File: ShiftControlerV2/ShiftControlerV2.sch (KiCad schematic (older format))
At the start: 24 parts, among them J1 Conn_02x06_Counter_Clockwise, J2 Conn_02x06_Counter_Clockwise, Q1 BTN8982TA, Q2 BTN8982TA, U1 ControllerBoardV2

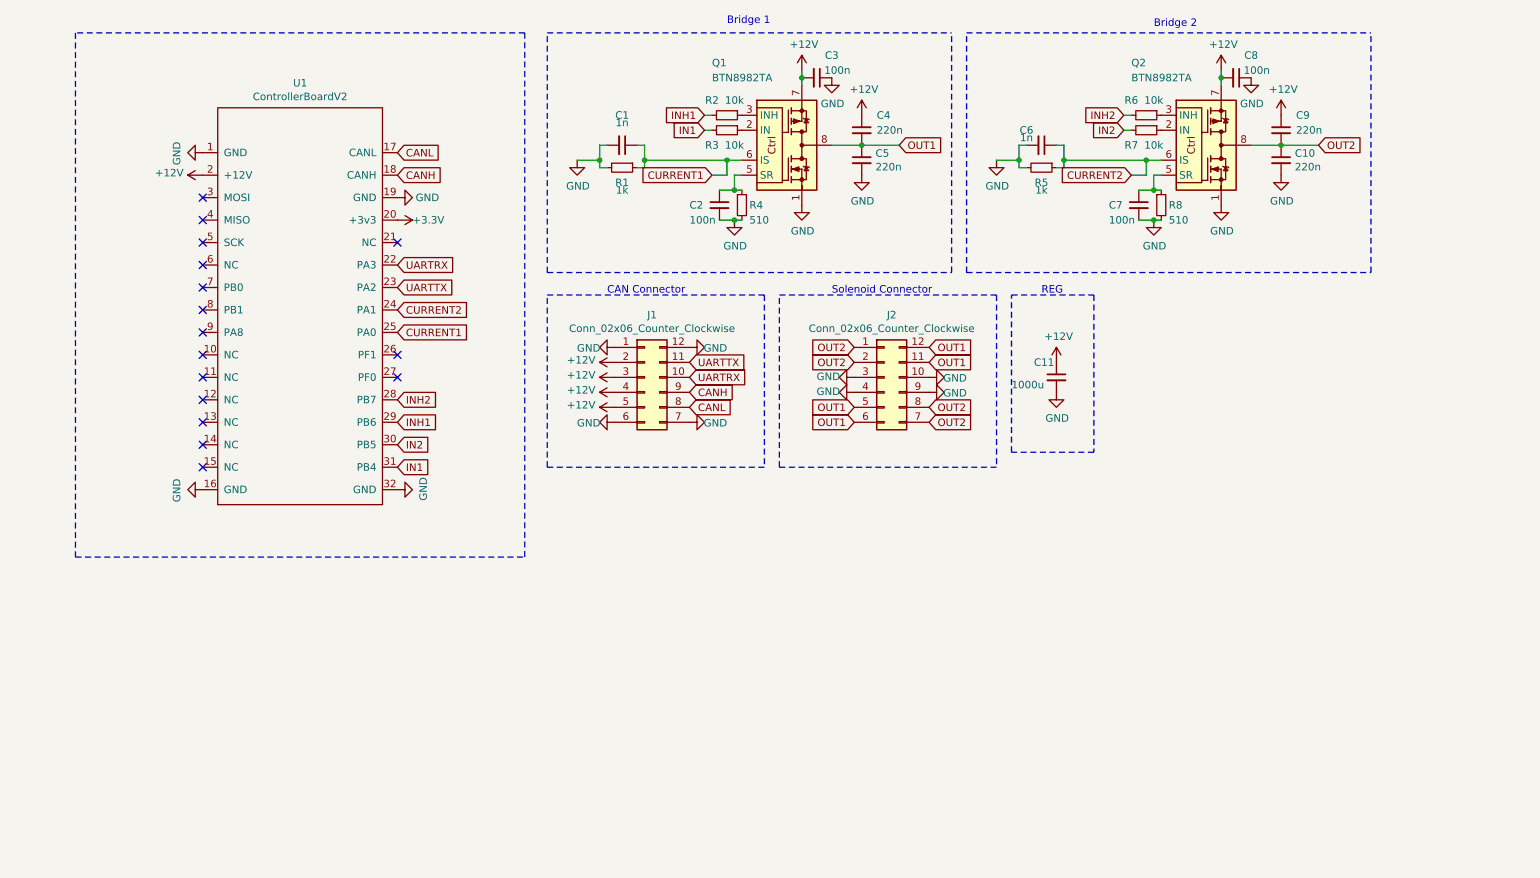
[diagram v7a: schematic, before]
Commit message: Update to provide additional power to micro
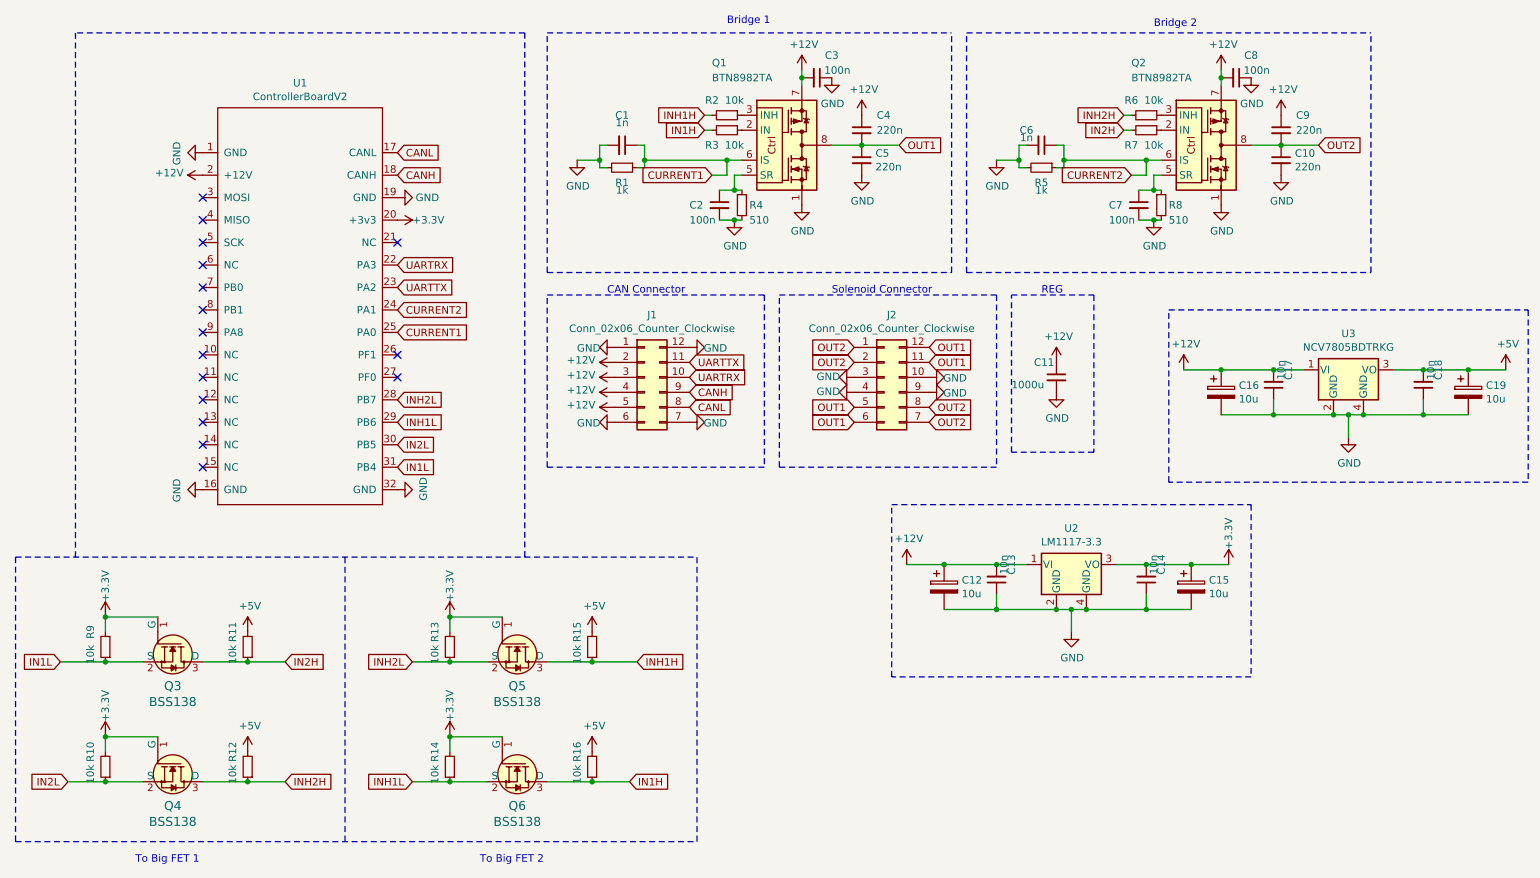
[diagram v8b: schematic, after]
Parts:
- added C12, C15, C16, C19: 10u, Capacitor_SMD:CP_Elec_5x4.4, symbol Device:CP
- added C13, C14, C17, C18: 10n, Capacitor_SMD:C_0603_1608Metric_Pad1.08x0.95mm_HandSolder, symbol Device:C_Small
- added Q3, Q4, Q5, Q6: BSS138, digikey-footprints:SOT-23-3, symbol dk_Transistors-FETs-MOSFETs-Single:BSS138
- added R10, R11, R12, R13, R14, R15, R16, R9: 10k, Resistor_SMD:R_0603_1608Metric_Pad0.98x0.95mm_HandSolder, symbol Device:R_Small
- added U2: LM1117-3.3, Package_TO_SOT_SMD:TO-252-3_TabPin4, symbol Lukas_Library:LM1117-3.3
- added U3: NCV7805BDTRKG, Package_TO_SOT_SMD:TO-252-3_TabPin4, symbol Lukas_Library:NCV7805BDTRKG
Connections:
- net +12V: now also C12.1, C13.2, C16.1, C17.2, U2.1 (VI), U3.1 (VI)
- net +3V3: now also C14.2, C15.1, Q3.1 (G), Q4.1 (G), Q5.1 (G), Q6.1 (G), R10.2, R13.2, R14.2, R9.2, U2.3 (VO)
- net GND: now also C12.2, C13.1, C14.1, C15.2, C16.2, C17.1, C18.1, C19.2, U2.2 (GND), U2.4 (GND), U3.2 (GND), U3.4 (GND)
- net IN1 renamed IN1H
- net IN1H: now also Q6.3 (D), R16.1; no longer U1.31 (PB4)
- net IN2 renamed IN2H
- net IN2H: now also Q3.3 (D), R11.1; no longer U1.30 (PB5)
- net INH1 renamed INH1H
- net INH1H: now also Q5.3 (D), R15.1; no longer U1.29 (PB6)
- net INH2 renamed INH2H
- net INH2H: now also Q4.3 (D), R12.1; no longer U1.28 (PB7)
- new net +5V: C18.2, C19.1, R11.2, R12.2, R15.2, R16.2, U3.3 (VO)
- new net IN1L: Q3.2 (S), R9.1, U1.31 (PB4)
- new net IN2L: Q4.2 (S), R10.1, U1.30 (PB5)
- new net INH1L: Q6.2 (S), R14.1, U1.29 (PB6)
- new net INH2L: Q5.2 (S), R13.1, U1.28 (PB7)
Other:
- note added: "To Big FET 1"
- note added: "To Big FET 2"
